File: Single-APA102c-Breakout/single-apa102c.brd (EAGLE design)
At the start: 15.2 x 17.4 mm, 4 parts, among them IC1 RE1C002UNTCL

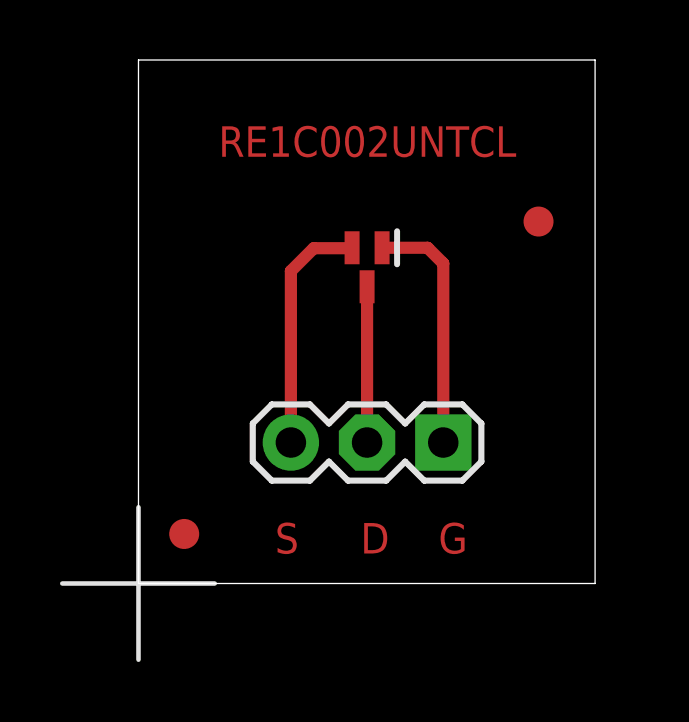
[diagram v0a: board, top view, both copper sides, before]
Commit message: infinity mirror single apa102c
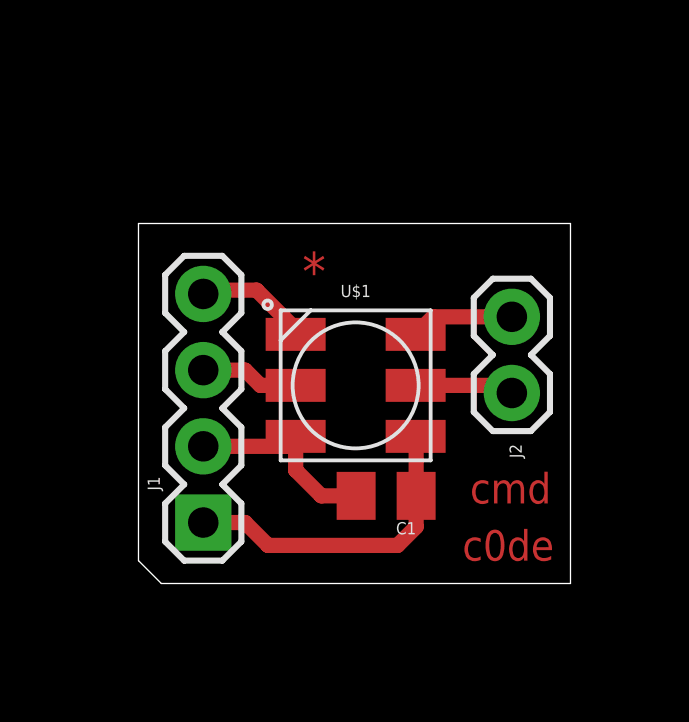
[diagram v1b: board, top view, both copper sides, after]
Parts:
- removed IC1: RE1C002UNTCL, transitors:SOT50P160X85-3N
- removed U$2, U$3: FIDUCIAL, adafruit:FIDUCIAL_1MM
- added C1: 15 pF, passives:C0805K
- added J1: (no value), connector:1X04
- added J2: (no value), connector:1X02
- U$1: value (none) -> APA1025050; device connector:1X03_UDPI -> leds:APA102_5050
- moved U$1 3.49 mm to (7.24, 6.60), turned to 0 degrees
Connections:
- removed net DRAIN: IC1.3, U$1.2
- removed net GATE: IC1.1, U$1.1
- removed net SRC: IC1.2, U$1.3
- new net CLKIN: J1.3, U$1.5
- new net CLKOUT: J2.2, U$1.2
- new net DATAIN: J1.4, U$1.4
- new net DATAOUT: J2.1, U$1.3
- new net GND: C1.2, J1.2, U$1.6
- new net VCC: C1.1, J1.1, U$1.1
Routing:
- net VCC: track 0.00 -> 10.7 mm
- net GATE: track 8.23 -> 0.00 mm
- net SRC: track 8.08 -> 0.00 mm
- net GND: track 0.00 -> 6.71 mm
- net DRAIN: track 5.19 -> 0.00 mm
- net DATAIN: track 0.00 -> 3.84 mm
- net DATAOUT: track 0.00 -> 3.45 mm
- net CLKOUT: track 0.00 -> 3.31 mm
- net CLKIN: track 0.00 -> 3.29 mm
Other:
- board size 15.2 x 17.4 mm -> 14.4 x 12 mm
- board text added: "*"
- board text added: "c0de"
- board text added: "cmd"
- board text removed: "D"
- board text removed: "G"
- board text removed: "RE1C002UNTCL"
- board text removed: "S"

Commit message: tweaking size to fit in infinity mirror
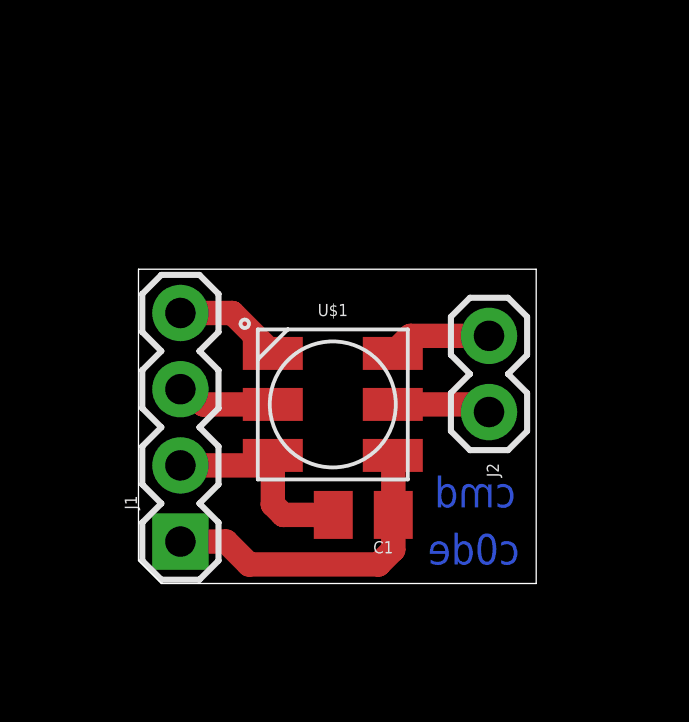
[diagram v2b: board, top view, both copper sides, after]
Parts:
- moved C1 0.99 mm to (7.49, 2.29)
- moved J2 0.99 mm to (11.7, 8.26)
- moved J1 0.99 mm to (1.40, 1.40)
- moved U$1 0.99 mm to (6.48, 5.97)
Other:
- board size 14.4 x 12 mm -> 13.3 x 10.5 mm
- board text removed: "*"
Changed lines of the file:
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@@
 <board>
 <plain>
-<wire x1="0.762" y1="0" x2="14.4" y2="0" width="0" layer="20"/>
-<wire x1="14.4" y1="0" x2="14.4" y2="12" width="0" layer="20"/>
-<wire x1="14.4" y1="12" x2="0" y2="12" width="0" layer="20"/>
-<wire x1="0" y1="12" x2="0" y2="0.762" width="0" layer="20"/>
+<wire x1="0.762" y1="0" x2="13.257" y2="0" width="0" layer="20"/>
+<wire x1="13.257" y1="0" x2="13.257" y2="10.476" width="0" layer="20"/>
+<wire x1="13.257" y1="10.476" x2="0" y2="10.476" width="0" layer="20"/>
+<wire x1="0" y1="10.476" x2="0" y2="0.762" width="0" layer="20"/>
 <wire x1="0.762" y1="0" x2="0" y2="0.762" width="0" layer="20"/>
-<text x="11.049" y="2.667" size="1.016" layer="1">cmd</text>
-<text x="10.795" y="0.762" size="1.016" layer="1">c0de</text>
-<text x="5.461" y="9.779" size="1.27" layer="1">*</text>
+<text x="12.573" y="2.54" size="1.016" layer="16" rot="MR0">cmd</text>
+<text x="12.7" y="0.635" size="1.016" layer="16" rot="MR0">c0de</text>
 </plain>
 <attributes>
@@
 </autorouter>
 <elements>
-<element name="C1" library="passives" package="C0805K" package3d_urn="urn:adsk.eagle:package:8089589/1" value="15 pF" x="8.255" y="2.921" smashed="yes" rot="R180">
-<attribute name="NAME" x="9.255" y="2.046" size="0.4064" layer="25" rot="R180"/>
-<attribute name="VALUE" x="9.001" y="4.44" size="0.4064" layer="27" rot="R180"/>
-</element>
-<element name="J1" library="connector" package="1X04" value="" x="2.159" y="2.032" smashed="yes" rot="R90">
-<attribute name="NAME" x="0.7112" y="3.0988" size="0.4064" layer="25" ratio="10" rot="R90"/>
-<attribute name="PROD_ID" value="CONN-09696" x="12.319" y="24.892" size="1.778" layer="27" rot="R90" display="off"/>
-<attribute name="VALUE" x="5.334" y="0.762" size="1.27" layer="27" rot="R90"/>
-</element>
-<element name="J2" library="connector" package="1X02" value="" x="12.446" y="8.89" smashed="yes" rot="R270">
-<attribute name="NAME" x="12.3698" y="4.6482" size="0.4064" layer="25" ratio="10" rot="R270"/>
-<attribute name="VALUE" x="9.271" y="10.16" size="1.27" layer="27" rot="R270"/>
-</element>
-<element name="U$1" library="leds" package="APA102_5050" package3d_urn="urn:adsk.eagle:package:15294973/2" value="APA1025050" x="7.239" y="6.604" smashed="yes">
-<attribute name="NAME" x="7.239" y="9.954" size="0.4064" layer="25" font="vector" rot="R180" align="bottom-center"/>
+<element name="C1" library="passives" package="C0805K" package3d_urn="urn:adsk.eagle:package:8089589/1" value="15 pF" x="7.493" y="2.286" smashed="yes" rot="R180">
+<attribute name="NAME" x="8.493" y="1.411" size="0.4064" layer="25" rot="R180"/>
+<attribute name="VALUE" x="7.223" y="3.678" size="0.4064" layer="27" rot="R180"/>
+</element>
+<element name="J1" library="connector" package="1X04" value="" x="1.397" y="1.397" smashed="yes" rot="R90">
+<attribute name="NAME" x="-0.0508" y="2.4638" size="0.4064" layer="25" ratio="10" rot="R90"/>
+<attribute name="PROD_ID" value="CONN-09696" x="11.557" y="24.257" size="1.778" layer="27" rot="R90" display="off"/>
+<attribute name="VALUE" x="4.572" y="0.127" size="1.27" layer="27" rot="R90"/>
+</element>
+<element name="J2" library="connector" package="1X02" value="" x="11.684" y="8.255" smashed="yes" rot="R270">
+<attribute name="NAME" x="11.6078" y="4.0132" size="0.4064" layer="25" ratio="10" rot="R270"/>
+<attribute name="VALUE" x="8.509" y="9.525" size="1.27" layer="27" rot="R270"/>
+</element>
+<element name="U$1" library="leds" package="APA102_5050" package3d_urn="urn:adsk.eagle:package:15294973/2" value="APA1025050" x="6.477" y="5.969" smashed="yes">
+<attribute name="NAME" x="6.477" y="9.319" size="0.4064" layer="25" font="vector" rot="R180" align="bottom-center"/>
 </element>
 </elements>
@@
 <contactref element="C1" pad="1"/>
 <contactref element="J1" pad="1"/>
-<wire x1="2.159" y1="2.032" x2="3.556" y2="2.032" width="0.508" layer="1"/>
-<wire x1="3.556" y1="2.032" x2="4.318" y2="1.27" width="0.508" layer="1"/>
-<wire x1="9.255" y1="1.889" x2="9.255" y2="2.921" width="0.508" layer="1"/>
-<wire x1="4.318" y1="1.27" x2="8.636" y2="1.27" width="0.508" layer="1"/>
-<wire x1="8.636" y1="1.27" x2="9.255" y2="1.889" width="0.508" layer="1"/>
-<wire x1="9.255" y1="2.921" x2="9.255" y2="4.888" width="0.508" layer="1"/>
-<wire x1="9.255" y1="4.888" x2="9.239" y2="4.904" width="0.508" layer="1"/>
+<wire x1="8.493" y1="4.253" x2="8.477" y2="4.269" width="0.508" layer="1"/>
+<wire x1="1.397" y1="1.397" x2="2.921" y2="1.397" width="0.8128" layer="1"/>
+<wire x1="8.493" y1="1.127" x2="8.493" y2="2.286" width="0.8128" layer="1"/>
+<wire x1="2.921" y1="1.397" x2="3.683" y2="0.635" width="0.8128" layer="1"/>
+<wire x1="3.683" y1="0.635" x2="8.001" y2="0.635" width="0.8128" layer="1"/>
+<wire x1="8.001" y1="0.635" x2="8.493" y2="1.127" width="0.8128" layer="1"/>
+<wire x1="8.493" y1="2.286" x2="8.493" y2="4.253" width="0.8128" layer="1"/>
 </signal>
 <signal name="GND">
@@
 <contactref element="C1" pad="2"/>
 <contactref element="J1" pad="2"/>
-<wire x1="2.159" y1="4.572" x2="4.907" y2="4.572" width="0.508" layer="1"/>
-<wire x1="4.907" y1="4.572" x2="5.239" y2="4.904" width="0.508" layer="1"/>
-<wire x1="7.255" y1="2.921" x2="6.096" y2="2.921" width="0.508" layer="1"/>
-<wire x1="6.096" y1="2.921" x2="5.239" y2="3.778" width="0.508" layer="1"/>
-<wire x1="5.239" y1="3.778" x2="5.239" y2="4.904" width="0.508" layer="1"/>
+<wire x1="4.477" y1="4.269" x2="4.477" y2="2.635" width="0.8128" layer="1"/>
+<wire x1="4.477" y1="2.635" x2="4.826" y2="2.286" width="0.8128" layer="1"/>
+<wire x1="4.826" y1="2.286" x2="6.493" y2="2.286" width="0.8128" layer="1"/>
+<wire x1="1.397" y1="3.937" x2="4.145" y2="3.937" width="0.8128" layer="1"/>
+<wire x1="4.145" y1="3.937" x2="4.477" y2="4.269" width="0.8128" layer="1"/>
 </signal>
 <signal name="DATAOUT">
 <contactref element="U$1" pad="3"/>
 <contactref element="J2" pad="1"/>
-<wire x1="9.239" y1="8.304" x2="9.825" y2="8.89" width="0.508" layer="1"/>
-<wire x1="9.825" y1="8.89" x2="12.446" y2="8.89" width="0.508" layer="1"/>
+<wire x1="8.477" y1="7.669" x2="9.063" y2="8.255" width="0.8128" layer="1"/>
+<wire x1="9.063" y1="8.255" x2="11.684" y2="8.255" width="0.8128" layer="1"/>
 </signal>
 <signal name="CLKOUT">
 <contactref element="U$1" pad="2"/>
 <contactref element="J2" pad="2"/>
-<wire x1="9.239" y1="6.604" x2="12.192" y2="6.604" width="0.508" layer="1"/>
-<wire x1="12.192" y1="6.604" x2="12.446" y2="6.35" width="0.508" layer="1"/>
+<wire x1="8.477" y1="5.969" x2="11.43" y2="5.969" width="0.8128" layer="1"/>
+<wire x1="11.43" y1="5.969" x2="11.684" y2="5.715" width="0.8128" layer="1"/>
 </signal>
 <signal name="DATAIN">
 <contactref element="U$1" pad="4"/>
 <contactref element="J1" pad="4"/>
-<wire x1="2.159" y1="9.652" x2="2.286" y2="9.779" width="0.508" layer="1"/>
-<wire x1="2.286" y1="9.779" x2="3.937" y2="9.779" width="0.508" layer="1"/>
-<wire x1="3.937" y1="9.779" x2="5.239" y2="8.477" width="0.508" layer="1"/>
-<wire x1="5.239" y1="8.477" x2="5.239" y2="8.304" width="0.508" layer="1"/>
+<wire x1="3.129" y1="9.017" x2="4.477" y2="7.669" width="0.8128" layer="1"/>
+<wire x1="1.397" y1="9.017" x2="3.129" y2="9.017" width="0.8128" layer="1"/>
 </signal>
 <signal name="CLKIN">
 <contactref element="U$1" pad="5"/>
 <contactref element="J1" pad="3"/>
-<wire x1="2.159" y1="7.112" x2="3.556" y2="7.112" width="0.508" layer="1"/>
-<wire x1="3.556" y1="7.112" x2="4.064" y2="6.604" width="0.508" layer="1"/>
-<wire x1="4.064" y1="6.604" x2="5.239" y2="6.604" width="0.508" layer="1"/>
+<wire x1="1.397" y1="6.477" x2="1.651" y2="6.477" width="0.8128" layer="1"/>
+<wire x1="1.651" y1="6.477" x2="2.159" y2="5.969" width="0.8128" layer="1"/>
+<wire x1="2.159" y1="5.969" x2="4.477" y2="5.969" width="0.8128" layer="1"/>
 </signal>
 </signals>

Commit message: angled apa102c to help with 3d printing
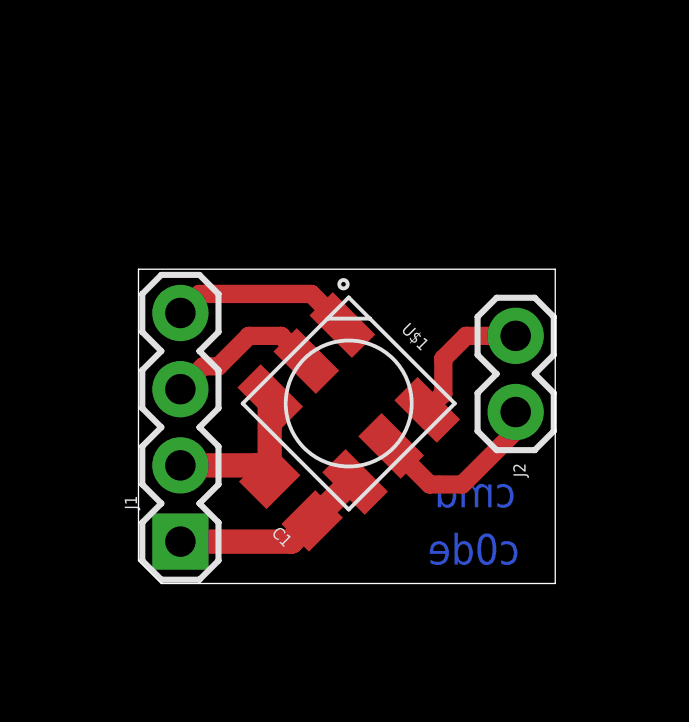
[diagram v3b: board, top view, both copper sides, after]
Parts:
- moved C1 2.47 mm to (5.08, 2.79), turned to 135 degrees
- moved J2 0.89 mm to (12.6, 8.26)
- moved U$1 0.53 mm to (7.01, 6.00), turned to 315 degrees
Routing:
- net VCC: track 10.8 -> 6.65 mm
- net CLKOUT: track 3.31 -> 6.05 mm
- net DATAIN: track 3.64 -> 6.09 mm
- net CLKIN: track 3.29 -> 5.28 mm
- net DATAOUT: track 3.45 -> 4.66 mm
- net GND: track 7.01 -> 5.88 mm
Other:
- board size 13.3 x 10.5 mm -> 13.9 x 10.5 mm
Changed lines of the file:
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@@
 <board>
 <plain>
-<wire x1="0.762" y1="0" x2="13.257" y2="0" width="0" layer="20"/>
-<wire x1="13.257" y1="0" x2="13.257" y2="10.476" width="0" layer="20"/>
-<wire x1="13.257" y1="10.476" x2="0" y2="10.476" width="0" layer="20"/>
+<wire x1="0.762" y1="0" x2="13.892" y2="0" width="0" layer="20"/>
+<wire x1="13.892" y1="0" x2="13.892" y2="10.476" width="0" layer="20"/>
+<wire x1="13.892" y1="10.476" x2="0" y2="10.476" width="0" layer="20"/>
 <wire x1="0" y1="10.476" x2="0" y2="0.762" width="0" layer="20"/>
 <wire x1="0.762" y1="0" x2="0" y2="0.762" width="0" layer="20"/>
@@
 </autorouter>
 <elements>
-<element name="C1" library="passives" package="C0805K" package3d_urn="urn:adsk.eagle:package:8089589/1" value="15 pF" x="7.493" y="2.286" smashed="yes" rot="R180">
-<attribute name="NAME" x="8.493" y="1.411" size="0.4064" layer="25" rot="R180"/>
-<attribute name="VALUE" x="7.223" y="3.678" size="0.4064" layer="27" rot="R180"/>
+<element name="C1" library="passives" package="C0805K" package3d_urn="urn:adsk.eagle:package:8089589/1" value="15 pF" x="5.08" y="2.794" smashed="yes" rot="R135">
+<attribute name="NAME" x="5.168390625" y="1.468175" size="0.4064" layer="25" rot="R135"/>
+<attribute name="VALUE" x="5.873375" y="3.969209375" size="0.4064" layer="27" rot="R135"/>
 </element>
 <element name="J1" library="connector" package="1X04" value="" x="1.397" y="1.397" smashed="yes" rot="R90">
@@
 <attribute name="VALUE" x="4.572" y="0.127" size="1.27" layer="27" rot="R90"/>
 </element>
-<element name="J2" library="connector" package="1X02" value="" x="11.684" y="8.255" smashed="yes" rot="R270">
-<attribute name="NAME" x="11.6078" y="4.0132" size="0.4064" layer="25" ratio="10" rot="R270"/>
-<attribute name="VALUE" x="8.509" y="9.525" size="1.27" layer="27" rot="R270"/>
-</element>
-<element name="U$1" library="leds" package="APA102_5050" package3d_urn="urn:adsk.eagle:package:15294973/2" value="APA1025050" x="6.477" y="5.969" smashed="yes">
-<attribute name="NAME" x="6.477" y="9.319" size="0.4064" layer="25" font="vector" rot="R180" align="bottom-center"/>
+<element name="J2" library="connector" package="1X02" value="" x="12.573" y="8.255" smashed="yes" rot="R270">
+<attribute name="NAME" x="12.4968" y="4.0132" size="0.4064" layer="25" ratio="10" rot="R270"/>
+<attribute name="VALUE" x="9.398" y="9.525" size="1.27" layer="27" rot="R270"/>
+</element>
+<element name="U$1" library="leds" package="APA102_5050" package3d_urn="urn:adsk.eagle:package:15294973/2" value="APA1025050" x="7.008" y="6" smashed="yes" rot="R315">
+<attribute name="NAME" x="9.37680625" y="8.368809375" size="0.4064" layer="25" font="vector" rot="R135" align="bottom-center"/>
 </element>
 </elements>
@@
 <contactref element="C1" pad="1"/>
 <contactref element="J1" pad="1"/>
-<wire x1="8.493" y1="4.253" x2="8.477" y2="4.269" width="0.508" layer="1"/>
-<wire x1="1.397" y1="1.397" x2="2.921" y2="1.397" width="0.8128" layer="1"/>
-<wire x1="8.493" y1="1.127" x2="8.493" y2="2.286" width="0.8128" layer="1"/>
-<wire x1="2.921" y1="1.397" x2="3.683" y2="0.635" width="0.8128" layer="1"/>
-<wire x1="3.683" y1="0.635" x2="8.001" y2="0.635" width="0.8128" layer="1"/>
-<wire x1="8.001" y1="0.635" x2="8.493" y2="1.127" width="0.8128" layer="1"/>
-<wire x1="8.493" y1="2.286" x2="8.493" y2="4.253" width="0.8128" layer="1"/>
+<wire x1="1.397" y1="1.397" x2="5.097215625" y2="1.397" width="0.8128" layer="1"/>
+<wire x1="5.097215625" y1="1.397" x2="5.78710625" y2="2.086890625" width="0.8128" layer="1"/>
+<wire x1="5.78710625" y1="2.086890625" x2="7.08391875" y2="3.383703125" width="0.8128" layer="1"/>
+<wire x1="7.08391875" y1="3.383703125" x2="7.22013125" y2="3.383703125" width="0.8128" layer="1"/>
 </signal>
 <signal name="GND">
@@
 <contactref element="C1" pad="2"/>
 <contactref element="J1" pad="2"/>
-<wire x1="4.477" y1="4.269" x2="4.477" y2="2.635" width="0.8128" layer="1"/>
-<wire x1="4.477" y1="2.635" x2="4.826" y2="2.286" width="0.8128" layer="1"/>
-<wire x1="4.826" y1="2.286" x2="6.493" y2="2.286" width="0.8128" layer="1"/>
-<wire x1="1.397" y1="3.937" x2="4.145" y2="3.937" width="0.8128" layer="1"/>
-<wire x1="4.145" y1="3.937" x2="4.477" y2="4.269" width="0.8128" layer="1"/>
+<wire x1="1.397" y1="3.937" x2="3.936996875" y2="3.937" width="0.8128" layer="1"/>
+<wire x1="3.936996875" y1="3.937" x2="4.372890625" y2="3.50110625" width="0.8128" layer="1"/>
+<wire x1="4.372890625" y1="3.50110625" x2="4.372890625" y2="6.19331875" width="0.8128" layer="1"/>
+<wire x1="4.372890625" y1="6.19331875" x2="4.391703125" y2="6.21213125" width="0.8128" layer="1"/>
 </signal>
 <signal name="DATAOUT">
 <contactref element="U$1" pad="3"/>
 <contactref element="J2" pad="1"/>
-<wire x1="8.477" y1="7.669" x2="9.063" y2="8.255" width="0.8128" layer="1"/>
-<wire x1="9.063" y1="8.255" x2="11.684" y2="8.255" width="0.8128" layer="1"/>
+<wire x1="9.62429375" y1="5.787865625" x2="10.16" y2="6.323571875" width="0.6096" layer="1"/>
+<wire x1="10.16" y1="6.323571875" x2="10.16" y2="7.493" width="0.6096" layer="1"/>
+<wire x1="10.16" y1="7.493" x2="10.922" y2="8.255" width="0.6096" layer="1"/>
+<wire x1="10.922" y1="8.255" x2="12.573" y2="8.255" width="0.6096" layer="1"/>
 </signal>
 <signal name="CLKOUT">
 <contactref element="U$1" pad="2"/>
 <contactref element="J2" pad="2"/>
-<wire x1="8.477" y1="5.969" x2="11.43" y2="5.969" width="0.8128" layer="1"/>
-<wire x1="11.43" y1="5.969" x2="11.684" y2="5.715" width="0.8128" layer="1"/>
+<wire x1="8.4222125" y1="4.585784375" x2="9.705996875" y2="3.302" width="0.6096" layer="1"/>
+<wire x1="9.705996875" y1="3.302" x2="10.795" y2="3.302" width="0.6096" layer="1"/>
+<wire x1="10.795" y1="3.302" x2="12.573" y2="5.08" width="0.6096" layer="1"/>
+<wire x1="12.573" y1="5.08" x2="12.573" y2="5.715" width="0.6096" layer="1"/>
 </signal>
 <signal name="DATAIN">
 <contactref element="U$1" pad="4"/>
 <contactref element="J1" pad="4"/>
-<wire x1="3.129" y1="9.017" x2="4.477" y2="7.669" width="0.8128" layer="1"/>
-<wire x1="1.397" y1="9.017" x2="3.129" y2="9.017" width="0.8128" layer="1"/>
+<wire x1="1.397" y1="9.017" x2="2.032" y2="9.652" width="0.6096" layer="1"/>
+<wire x1="5.760159375" y1="9.652" x2="6.795865625" y2="8.61629375" width="0.6096" layer="1"/>
+<wire x1="2.032" y1="9.652" x2="5.760159375" y2="9.652" width="0.6096" layer="1"/>
 </signal>
 <signal name="CLKIN">
 <contactref element="U$1" pad="5"/>
 <contactref element="J1" pad="3"/>
-<wire x1="1.397" y1="6.477" x2="1.651" y2="6.477" width="0.8128" layer="1"/>
-<wire x1="1.651" y1="6.477" x2="2.159" y2="5.969" width="0.8128" layer="1"/>
-<wire x1="2.159" y1="5.969" x2="4.477" y2="5.969" width="0.8128" layer="1"/>
+<wire x1="1.397" y1="6.477" x2="2.159" y2="7.239" width="0.6096" layer="1"/>
+<wire x1="2.667" y1="7.239" x2="3.683" y2="8.255" width="0.6096" layer="1"/>
+<wire x1="3.683" y1="8.255" x2="4.752996875" y2="8.255" width="0.6096" layer="1"/>
+<wire x1="4.752996875" y1="8.255" x2="5.593784375" y2="7.4142125" width="0.6096" layer="1"/>
+<wire x1="2.159" y1="7.239" x2="2.667" y2="7.239" width="0.6096" layer="1"/>
 </signal>
 </signals>

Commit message: moved led to a 45 degree angle
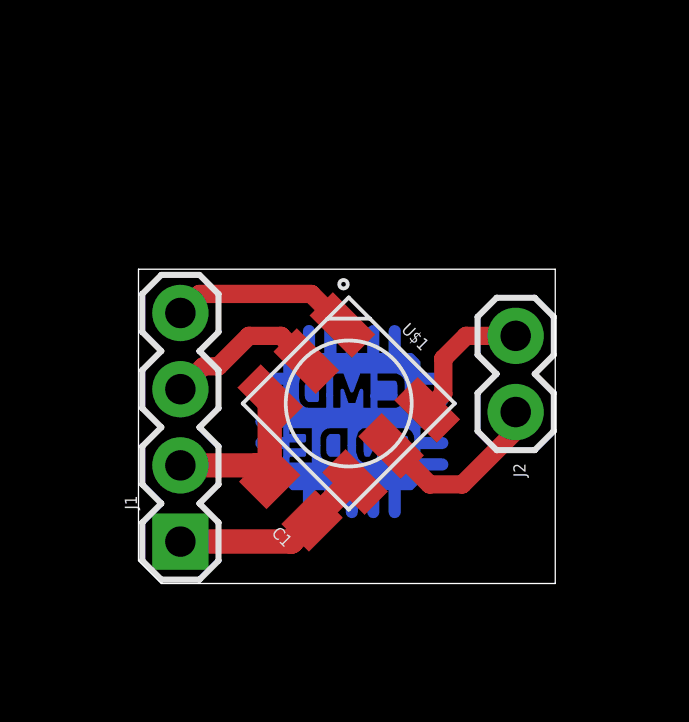
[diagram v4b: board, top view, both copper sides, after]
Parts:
- added U$2: CMD_C0DE_LOGOCMD_CODE_LOGO_TOP_COPPER, logos:CMD_C0DE_LOGO_TOP_COPPER
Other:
- board text removed: "c0de"
- board text removed: "cmd"
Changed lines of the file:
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@@
 <wire x1="0" y1="10.476" x2="0" y2="0.762" width="0" layer="20"/>
 <wire x1="0.762" y1="0" x2="0" y2="0.762" width="0" layer="20"/>
-<text x="12.573" y="2.54" size="1.016" layer="16" rot="MR0">cmd</text>
-<text x="12.7" y="0.635" size="1.016" layer="16" rot="MR0">c0de</text>
 </plain>
 <attributes>
@@
 <attribute name="NAME" x="9.37680625" y="8.368809375" size="0.4064" layer="25" font="vector" rot="R135" align="bottom-center"/>
 </element>
+<element name="U$2" library="logos" package="CMD_C0DE_LOGO_TOP_COPPER" value="CMD_C0DE_LOGOCMD_CODE_LOGO_TOP_COPPER" x="7.112" y="5.715" smashed="yes" rot="MR0"/>
 </elements>
 <signals>
